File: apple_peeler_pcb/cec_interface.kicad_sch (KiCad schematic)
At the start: 7 parts, among them Q13 2N7002

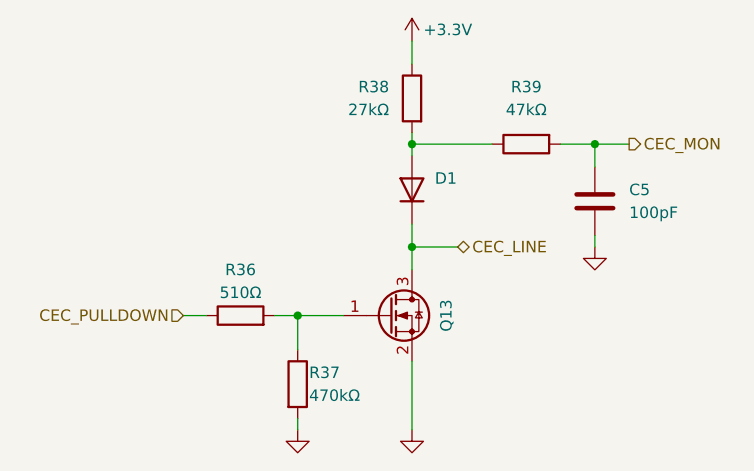
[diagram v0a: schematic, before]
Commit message: we paid for all the pins, we're gonna use all the pins
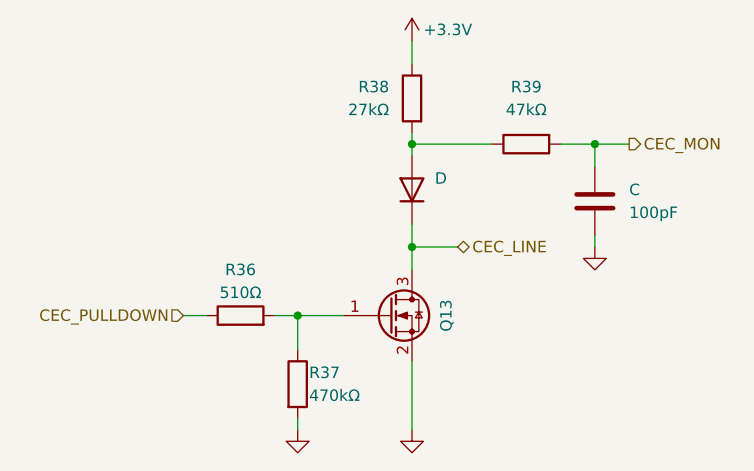
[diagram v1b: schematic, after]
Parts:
- renumbered C5 to C, D1 to D
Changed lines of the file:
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@@
+					(unit 1)
+				)
+				(path "/d5946b96-44a8-4a28-8641-19803e1510af/ab4760da-4146-4688-a275-418314974b55/9898d91a-fb1c-440b-9509-02fc004394d7"
+					(reference "R?")
 					(unit 1)
 				)
@@
 		(dnp no)
 		(fields_autoplaced yes)
-		(property "Reference" "C5"
+		(property "Reference" "C"
 			(at 158.75 96.5199 0)
 			(effects
@@
 		)
 		(instances
-			(project ""
-				(path "/d5946b96-44a8-4a28-8641-19803e1510af/ab4760da-4146-4688-a275-418314974b55/81932bd6-0e7a-4e3b-bdf1-28d2dccc0222"
-					(reference "C5")
+			(project "apple_peeler_pcb"
+				(path "/d5946b96-44a8-4a28-8641-19803e1510af/ab4760da-4146-4688-a275-418314974b55/9898d91a-fb1c-440b-9509-02fc004394d7"
+					(reference "C?")
 					(unit 1)
 				)
@@
 		(dnp no)
 		(fields_autoplaced yes)
-		(property "Reference" "D1"
+		(property "Reference" "D"
 			(at 137.16 95.2499 90)
 			(effects
@@
 		)
 		(instances
-			(project ""
-				(path "/d5946b96-44a8-4a28-8641-19803e1510af/ab4760da-4146-4688-a275-418314974b55/81932bd6-0e7a-4e3b-bdf1-28d2dccc0222"
-					(reference "D1")
+			(project "apple_peeler_pcb"
+				(path "/d5946b96-44a8-4a28-8641-19803e1510af/ab4760da-4146-4688-a275-418314974b55/9898d91a-fb1c-440b-9509-02fc004394d7"
+					(reference "D?")
 					(unit 1)
 				)
@@
 					(unit 1)
 				)
+				(path "/d5946b96-44a8-4a28-8641-19803e1510af/ab4760da-4146-4688-a275-418314974b55/9898d91a-fb1c-440b-9509-02fc004394d7"
+					(reference "#PWR0110")
+					(unit 1)
+				)
 			)
 		)
@@
 					(unit 1)
 				)
+				(path "/d5946b96-44a8-4a28-8641-19803e1510af/ab4760da-4146-4688-a275-418314974b55/9898d91a-fb1c-440b-9509-02fc004394d7"
+					(reference "#PWR0108")
+					(unit 1)
+				)
 			)
 		)
@@
 					(unit 1)
 				)
+				(path "/d5946b96-44a8-4a28-8641-19803e1510af/ab4760da-4146-4688-a275-418314974b55/9898d91a-fb1c-440b-9509-02fc004394d7"
+					(reference "R?")
+					(unit 1)
+				)
 			)
 		)
@@
 				(path "/d5946b96-44a8-4a28-8641-19803e1510af/ab4760da-4146-4688-a275-418314974b55/81932bd6-0e7a-4e3b-bdf1-28d2dccc0222"
 					(reference "#PWR057")
+					(unit 1)
+				)
+				(path "/d5946b96-44a8-4a28-8641-19803e1510af/ab4760da-4146-4688-a275-418314974b55/9898d91a-fb1c-440b-9509-02fc004394d7"
+					(reference "#PWR0107")
 					(unit 1)
 				)
@@
 					(unit 1)
 				)
+				(path "/d5946b96-44a8-4a28-8641-19803e1510af/ab4760da-4146-4688-a275-418314974b55/9898d91a-fb1c-440b-9509-02fc004394d7"
+					(reference "R?")
+					(unit 1)
+				)
 			)
 		)
@@
 					(unit 1)
 				)
+				(path "/d5946b96-44a8-4a28-8641-19803e1510af/ab4760da-4146-4688-a275-418314974b55/9898d91a-fb1c-440b-9509-02fc004394d7"
+					(reference "#PWR0109")
+					(unit 1)
+				)
 			)
 		)
@@
 					(unit 1)
 				)
+				(path "/d5946b96-44a8-4a28-8641-19803e1510af/ab4760da-4146-4688-a275-418314974b55/9898d91a-fb1c-440b-9509-02fc004394d7"
+					(reference "Q?")
+					(unit 1)
+				)
 			)
 		)
@@
 					(unit 1)
 				)
+				(path "/d5946b96-44a8-4a28-8641-19803e1510af/ab4760da-4146-4688-a275-418314974b55/9898d91a-fb1c-440b-9509-02fc004394d7"
+					(reference "R?")
+					(unit 1)
+				)

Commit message: use wleds instead of individual leds
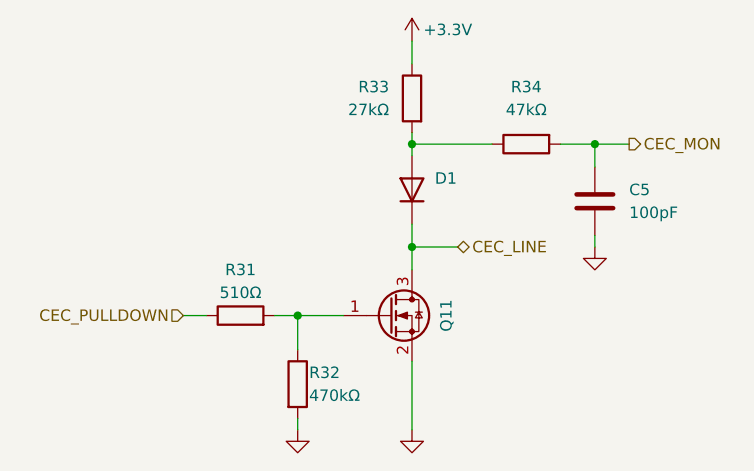
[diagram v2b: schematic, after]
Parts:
- renumbered C to C5, D to D1, Q13 to Q11, R36 to R31, R37 to R32, R38 to R33, R39 to R34
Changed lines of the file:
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@@
 		(dnp no)
 		(fields_autoplaced yes)
-		(property "Reference" "R38"
+		(property "Reference" "R33"
 			(at 132.08 85.0899 0)
 			(effects
@@
 			(project "apple_peeler_pcb"
 				(path "/d5946b96-44a8-4a28-8641-19803e1510af/ab4760da-4146-4688-a275-418314974b55/81932bd6-0e7a-4e3b-bdf1-28d2dccc0222"
-					(reference "R38")
-					(unit 1)
-				)
-				(path "/d5946b96-44a8-4a28-8641-19803e1510af/ab4760da-4146-4688-a275-418314974b55/9898d91a-fb1c-440b-9509-02fc004394d7"
-					(reference "R?")
+					(reference "R33")
+					(unit 1)
+				)
+				(path "/d5946b96-44a8-4a28-8641-19803e1510af/ab4760da-4146-4688-a275-418314974b55/9898d91a-fb1c-440b-9509-02fc004394d7"
+					(reference "R59")
 					(unit 1)
 				)
@@
 		(dnp no)
 		(fields_autoplaced yes)
-		(property "Reference" "C"
+		(property "Reference" "C5"
 			(at 158.75 96.5199 0)
 			(effects
@@
 		(instances
 			(project "apple_peeler_pcb"
-				(path "/d5946b96-44a8-4a28-8641-19803e1510af/ab4760da-4146-4688-a275-418314974b55/9898d91a-fb1c-440b-9509-02fc004394d7"
-					(reference "C?")
+				(path "/d5946b96-44a8-4a28-8641-19803e1510af/ab4760da-4146-4688-a275-418314974b55/81932bd6-0e7a-4e3b-bdf1-28d2dccc0222"
+					(reference "C5")
+					(unit 1)
+				)
+				(path "/d5946b96-44a8-4a28-8641-19803e1510af/ab4760da-4146-4688-a275-418314974b55/9898d91a-fb1c-440b-9509-02fc004394d7"
+					(reference "C24")
 					(unit 1)
 				)
@@
 		(dnp no)
 		(fields_autoplaced yes)
-		(property "Reference" "D"
+		(property "Reference" "D1"
 			(at 137.16 95.2499 90)
 			(effects
@@
 		(instances
 			(project "apple_peeler_pcb"
-				(path "/d5946b96-44a8-4a28-8641-19803e1510af/ab4760da-4146-4688-a275-418314974b55/9898d91a-fb1c-440b-9509-02fc004394d7"
-					(reference "D?")
+				(path "/d5946b96-44a8-4a28-8641-19803e1510af/ab4760da-4146-4688-a275-418314974b55/81932bd6-0e7a-4e3b-bdf1-28d2dccc0222"
+					(reference "D1")
+					(unit 1)
+				)
+				(path "/d5946b96-44a8-4a28-8641-19803e1510af/ab4760da-4146-4688-a275-418314974b55/9898d91a-fb1c-440b-9509-02fc004394d7"
+					(reference "D7")
 					(unit 1)
 				)
@@
 		(on_board yes)
 		(dnp no)
-		(property "Reference" "#PWR060"
+		(property "Reference" "#PWR055"
 			(at 154.94 109.22 0)
 			(effects
@@
 			(project "apple_peeler_pcb"
 				(path "/d5946b96-44a8-4a28-8641-19803e1510af/ab4760da-4146-4688-a275-418314974b55/81932bd6-0e7a-4e3b-bdf1-28d2dccc0222"
-					(reference "#PWR060")
-					(unit 1)
-				)
-				(path "/d5946b96-44a8-4a28-8641-19803e1510af/ab4760da-4146-4688-a275-418314974b55/9898d91a-fb1c-440b-9509-02fc004394d7"
-					(reference "#PWR0110")
+					(reference "#PWR055")
+					(unit 1)
+				)
+				(path "/d5946b96-44a8-4a28-8641-19803e1510af/ab4760da-4146-4688-a275-418314974b55/9898d91a-fb1c-440b-9509-02fc004394d7"
+					(reference "#PWR0111")
 					(unit 1)
 				)
@@
 		(on_board yes)
 		(dnp no)
-		(property "Reference" "#PWR058"
+		(property "Reference" "#PWR053"
 			(at 134.62 83.82 0)
 			(effects
@@
 			(project "apple_peeler_pcb"
 				(path "/d5946b96-44a8-4a28-8641-19803e1510af/ab4760da-4146-4688-a275-418314974b55/81932bd6-0e7a-4e3b-bdf1-28d2dccc0222"
-					(reference "#PWR058")
-					(unit 1)
-				)
-				(path "/d5946b96-44a8-4a28-8641-19803e1510af/ab4760da-4146-4688-a275-418314974b55/9898d91a-fb1c-440b-9509-02fc004394d7"
-					(reference "#PWR0108")
+					(reference "#PWR053")
+					(unit 1)
+				)
+				(path "/d5946b96-44a8-4a28-8641-19803e1510af/ab4760da-4146-4688-a275-418314974b55/9898d91a-fb1c-440b-9509-02fc004394d7"
+					(reference "#PWR0109")
 					(unit 1)
 				)
@@
 		(on_board yes)
 		(dnp no)
-		(property "Reference" "R36"
+		(property "Reference" "R31"
 			(at 115.57 105.41 90)
 			(effects
@@
 			(project "apple_peeler_pcb"
 				(path "/d5946b96-44a8-4a28-8641-19803e1510af/ab4760da-4146-4688-a275-418314974b55/81932bd6-0e7a-4e3b-bdf1-28d2dccc0222"
-					(reference "R36")
-					(unit 1)
-				)
-				(path "/d5946b96-44a8-4a28-8641-19803e1510af/ab4760da-4146-4688-a275-418314974b55/9898d91a-fb1c-440b-9509-02fc004394d7"
-					(reference "R?")
+					(reference "R31")
+					(unit 1)
+				)
+				(path "/d5946b96-44a8-4a28-8641-19803e1510af/ab4760da-4146-4688-a275-418314974b55/9898d91a-fb1c-440b-9509-02fc004394d7"
+					(reference "R57")
 					(unit 1)
 				)
@@
 		(on_board yes)
 		(dnp no)
-		(property "Reference" "#PWR057"
+		(property "Reference" "#PWR052"
 			(at 121.92 129.54 0)
 			(effects
@@
 			(project "apple_peeler_pcb"
 				(path "/d5946b96-44a8-4a28-8641-19803e1510af/ab4760da-4146-4688-a275-418314974b55/81932bd6-0e7a-4e3b-bdf1-28d2dccc0222"
-					(reference "#PWR057")
-					(unit 1)
-				)
-				(path "/d5946b96-44a8-4a28-8641-19803e1510af/ab4760da-4146-4688-a275-418314974b55/9898d91a-fb1c-440b-9509-02fc004394d7"
-					(reference "#PWR0107")
+					(reference "#PWR052")
+					(unit 1)
+				)
+				(path "/d5946b96-44a8-4a28-8641-19803e1510af/ab4760da-4146-4688-a275-418314974b55/9898d91a-fb1c-440b-9509-02fc004394d7"
+					(reference "#PWR0108")
 					(unit 1)
 				)
@@
 		(dnp no)
 		(fields_autoplaced yes)
-		(property "Reference" "R39"
+		(property "Reference" "R34"
 			(at 147.32 85.09 90)
 			(effects
@@
 			(project "apple_peeler_pcb"
 				(path "/d5946b96-44a8-4a28-8641-19803e1510af/ab4760da-4146-4688-a275-418314974b55/81932bd6-0e7a-4e3b-bdf1-28d2dccc0222"
-					(reference "R39")
-					(unit 1)
-				)
-				(path "/d5946b96-44a8-4a28-8641-19803e1510af/ab4760da-4146-4688-a275-418314974b55/9898d91a-fb1c-440b-9509-02fc004394d7"
-					(reference "R?")
+					(reference "R34")
+					(unit 1)
+				)
+				(path "/d5946b96-44a8-4a28-8641-19803e1510af/ab4760da-4146-4688-a275-418314974b55/9898d91a-fb1c-440b-9509-02fc004394d7"
+					(reference "R60")
 					(unit 1)
 				)
@@
 		(on_board yes)
 		(dnp no)
-		(property "Reference" "#PWR059"
+		(property "Reference" "#PWR054"
 			(at 134.62 129.54 0)
 			(effects
@@
 			(project "apple_peeler_pcb"
 				(path "/d5946b96-44a8-4a28-8641-19803e1510af/ab4760da-4146-4688-a275-418314974b55/81932bd6-0e7a-4e3b-bdf1-28d2dccc0222"
-					(reference "#PWR059")
-					(unit 1)
-				)
-				(path "/d5946b96-44a8-4a28-8641-19803e1510af/ab4760da-4146-4688-a275-418314974b55/9898d91a-fb1c-440b-9509-02fc004394d7"
-					(reference "#PWR0109")
+					(reference "#PWR054")
+					(unit 1)
+				)
+				(path "/d5946b96-44a8-4a28-8641-19803e1510af/ab4760da-4146-4688-a275-418314974b55/9898d91a-fb1c-440b-9509-02fc004394d7"
+					(reference "#PWR0110")
 					(unit 1)
 				)
@@
 		(on_board yes)
 		(dnp no)
-		(property "Reference" "Q13"
+		(property "Reference" "Q11"
 			(at 138.43 110.49 90)
 			(effects
@@
 			(project "apple_peeler_pcb"
 				(path "/d5946b96-44a8-4a28-8641-19803e1510af/ab4760da-4146-4688-a275-418314974b55/81932bd6-0e7a-4e3b-bdf1-28d2dccc0222"
-					(reference "Q13")
-					(unit 1)
-				)
-				(path "/d5946b96-44a8-4a28-8641-19803e1510af/ab4760da-4146-4688-a275-418314974b55/9898d91a-fb1c-440b-9509-02fc004394d7"
-					(reference "Q?")
+					(reference "Q11")
+					(unit 1)
+				)
+				(path "/d5946b96-44a8-4a28-8641-19803e1510af/ab4760da-4146-4688-a275-418314974b55/9898d91a-fb1c-440b-9509-02fc004394d7"
+					(reference "Q17")
 					(unit 1)
 				)
@@
 		(on_board yes)
 		(dnp no)
-		(property "Reference" "R37"
+		(property "Reference" "R32"
 			(at 123.19 116.84 0)
 			(effects
@@
 			(project "apple_peeler_pcb"
 				(path "/d5946b96-44a8-4a28-8641-19803e1510af/ab4760da-4146-4688-a275-418314974b55/81932bd6-0e7a-4e3b-bdf1-28d2dccc0222"
-					(reference "R37")
-					(unit 1)
-				)
-				(path "/d5946b96-44a8-4a28-8641-19803e1510af/ab4760da-4146-4688-a275-418314974b55/9898d91a-fb1c-440b-9509-02fc004394d7"
-					(reference "R?")
-					(unit 1)
-				)
+					(reference "R32")
+					(unit 1)
+				)
+				(path "/d5946b96-44a8-4a28-8641-19803e1510af/ab4760da-4146-4688-a275-418314974b55/9898d91a-fb1c-440b-9509-02fc004394d7"
+					(reference "R58")
+					(unit 1)
+				)
